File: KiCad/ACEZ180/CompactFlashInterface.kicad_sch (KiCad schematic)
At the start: 29 parts

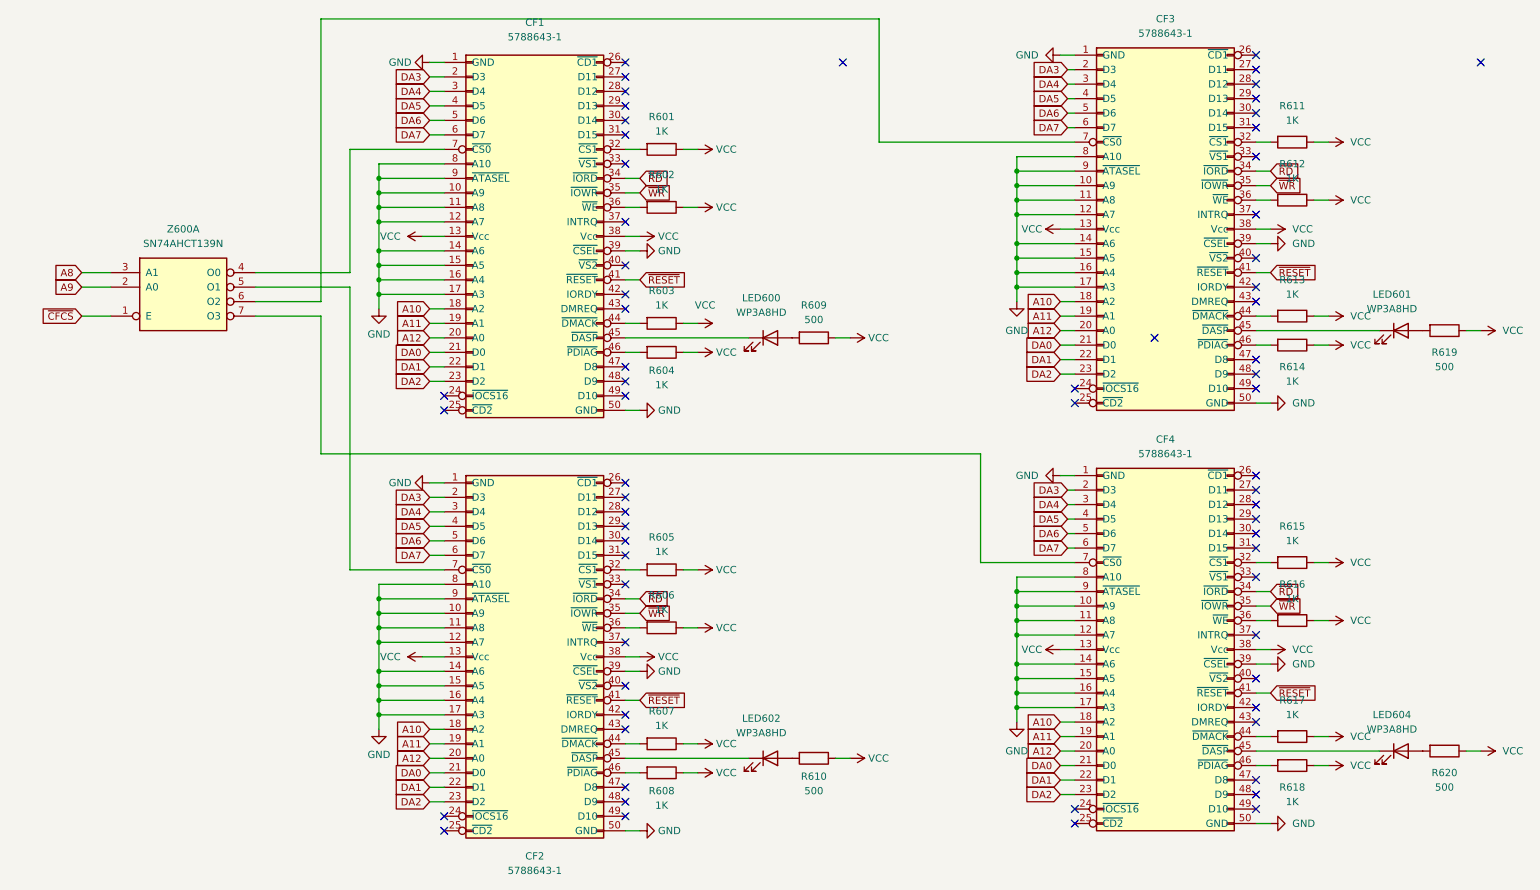
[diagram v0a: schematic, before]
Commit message: Fix mistake with ROM Select.
Signed-off-by: John Bradley <flypie@rocketmail.com>
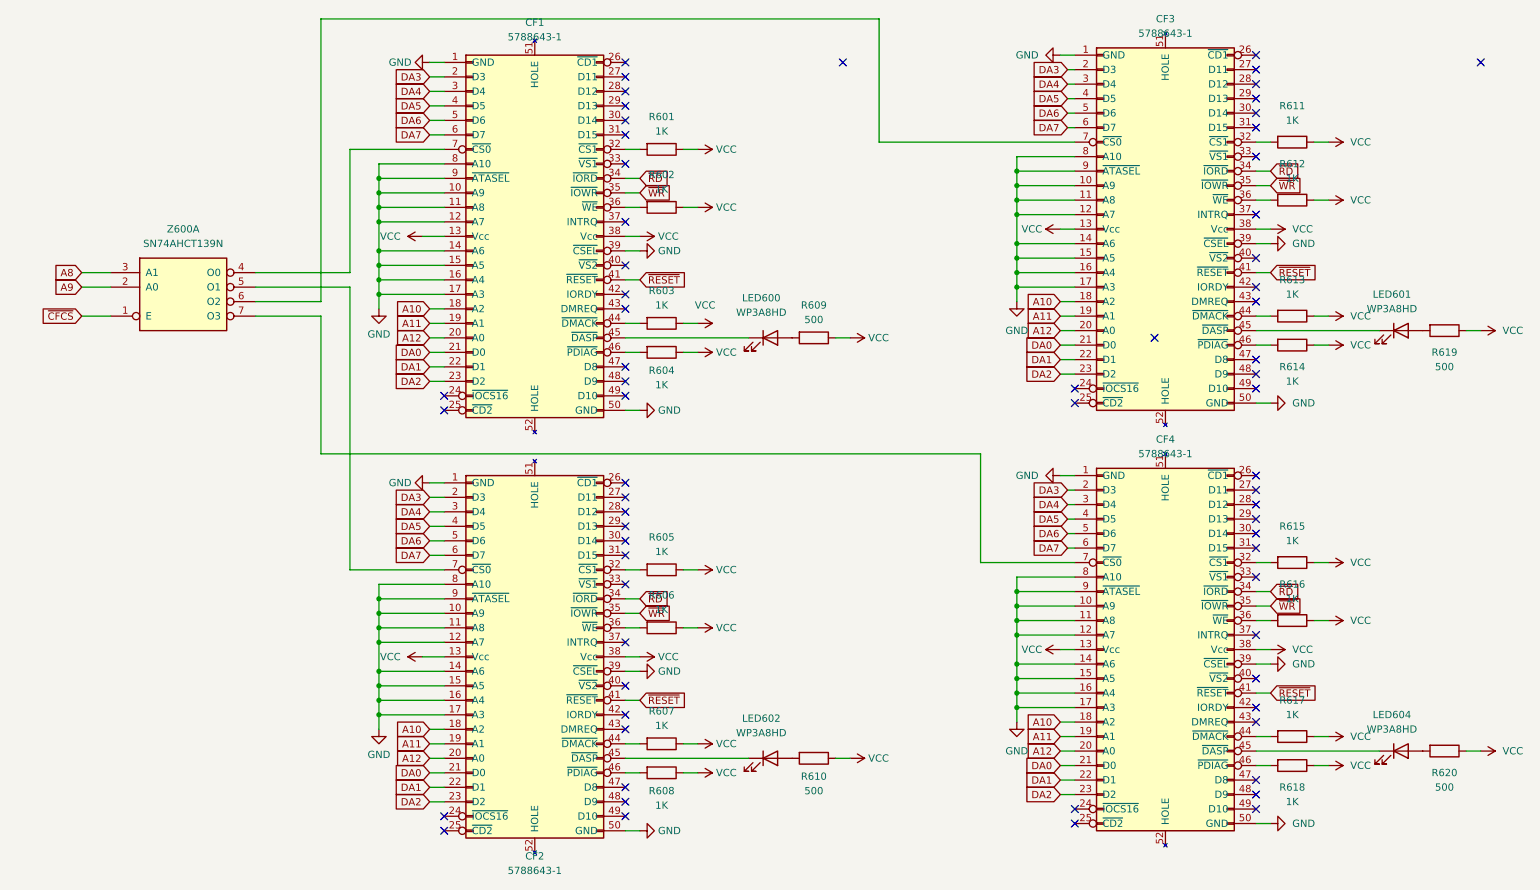
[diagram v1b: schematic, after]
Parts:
- CF1, CF2, CF3, CF4: footprint (none) -> ExtraFootprints:57886431
- LED600, LED601, LED602, LED604: footprint (none) -> LED_THT:LED_D3.0mm
- R601, R602, R603, R604, R605, R606, R607, R608, R609, R610, R611, R612, R613, R614, R615, R616, R617, R618, R619, R620: footprint (none) -> Resistor_THT:R_Axial_DIN0204_L3.6mm_D1.6mm_P2.54mm_Vertical
